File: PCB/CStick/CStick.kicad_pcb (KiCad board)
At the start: 2 copper layers, 39.1 x 31.5 mm, 4 parts, among them J1 Conn_01x04_Male, U1 Stickbox_Assembly

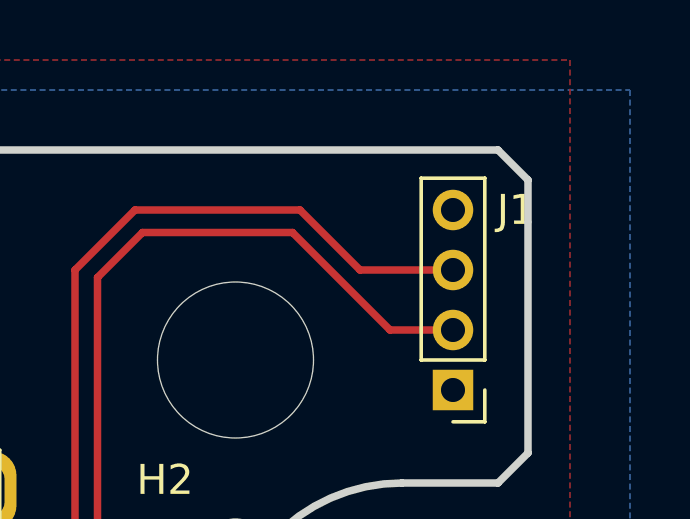
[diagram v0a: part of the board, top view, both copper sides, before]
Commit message: More cleanup and teaking of the PCBs, made BOM and placement files for JLC
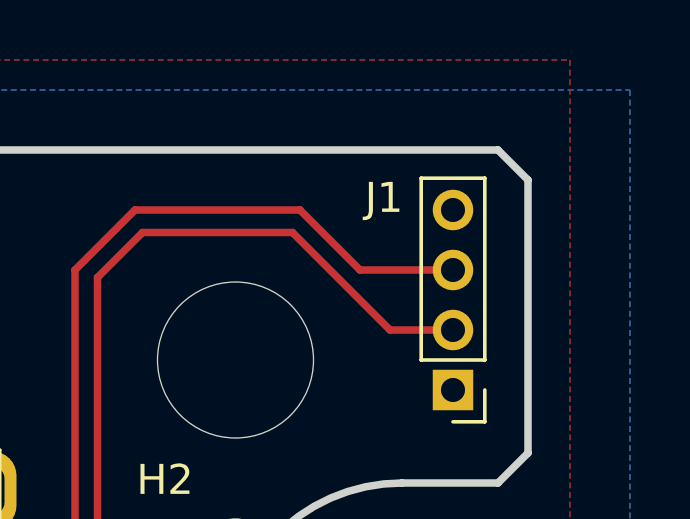
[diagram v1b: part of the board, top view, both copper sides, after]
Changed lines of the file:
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@@
     (grid_origin 150 100)
     (pcbplotparams
-      (layerselection 0x00010fc_ffffffff)
+      (layerselection 0x00010f0_ffffffff)
       (disableapertmacros false)
       (usegerberextensions false)
@@
       (outputformat 1)
       (mirror false)
-      (drillshape 1)
+      (drillshape 0)
       (scaleselection 1)
-      (outputdirectory "")
+      (outputdirectory "JLCPCB")
     )
   )
@@
     (property "Sheetname" "")
     (attr through_hole)
-    (fp_text reference "J1" (at -2.1 6) (layer "F.SilkS")
+    (fp_text reference "J1" (at 2.3 6.4) (layer "F.SilkS")
       (effects (font (size 1 1) (thickness 0.15)))
     )
